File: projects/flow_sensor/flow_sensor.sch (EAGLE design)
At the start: 81 parts, among them IC1 TPS61201, IC5 REG1118

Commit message: Resubmitting work for 1/24/18
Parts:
- added U$5: LM321, my_library:LM321
- U$8: value AD8295 -> INA826; device my_library:AD8295 -> my_library:INA826
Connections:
- removed net N$35: C41.1, R8.2, R9.1
- removed net N$48: C41.2, U$8.+IN, U$8.A2-IN, U$8.A2OUT
- new net N$31: C41.1, U$5.IN-, U$5.VOUT, U$8.IN+
- new net N$36: C41.2, R8.2, R9.1
- net 3.3V: now also U$5.VCC-, U$8.IN-, U$8.REF, U$8.VS-; no longer U$8.-IN
- net N$19: now also U$5.IN+; no longer U$8.A2+IN
- net SENSOR_OUT: now also U$8.VOUT; no longer U$8.OUT
- net VCC: now also U$5.VCC+, U$8.VS+
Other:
- moved on the sheet: C41, R36
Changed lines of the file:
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@@
 <part name="U$7" library="my_library" deviceset="MAX4634" device=""/>
 <part name="GND35" library="SparkFun-PowerSymbols" deviceset="GND2" device=""/>
-<part name="U$8" library="my_library" deviceset="AD8295" device=""/>
 <part name="C41" library="SparkFun-Capacitors" deviceset="4.7UF" device="0603" value="3uF"/>
 <part name="GND36" library="SparkFun-PowerSymbols" deviceset="GND2" device=""/>
 <part name="R36" library="SparkFun-Resistors" deviceset="787OHM" device="-0603-1/10W-1%" value="600"/>
+<part name="U$5" library="my_library" deviceset="LM321" device=""/>
+<part name="GND22" library="SparkFun-PowerSymbols" deviceset="GND2" device=""/>
+<part name="U$8" library="my_library" deviceset="INA826" device=""/>
+<part name="GND28" library="SparkFun-PowerSymbols" deviceset="GND2" device=""/>
 </parts>
 <sheets>
@@
 <instance part="U$7" gate="G$1" x="254" y="5.08"/>
 <instance part="GND35" gate="G$1" x="256.54" y="27.94" rot="R180"/>
-<instance part="U$8" gate="G$1" x="337.82" y="-5.08" rot="R90"/>
-<instance part="C41" gate="G$1" x="302.26" y="15.24" rot="R90"/>
-<instance part="GND36" gate="G$1" x="322.58" y="-27.94" rot="R270"/>
-<instance part="R36" gate="G$1" x="330.2" y="-35.56"/>
+<instance part="C41" gate="G$1" x="302.26" y="-7.62" rot="R270"/>
+<instance part="GND36" gate="G$1" x="398.78" y="0" rot="R90"/>
+<instance part="R36" gate="G$1" x="383.54" y="-10.16"/>
+<instance part="U$5" gate="G$1" x="335.28" y="-2.54"/>
+<instance part="GND22" gate="G$1" x="340.36" y="-20.32"/>
+<instance part="U$8" gate="G$1" x="383.54" y="12.7" rot="R90"/>
+<instance part="GND28" gate="G$1" x="403.86" y="15.24" rot="R90"/>
 </instances>
 <busses>
@@
 <label x="251.46" y="25.4" size="1.778" layer="95" rot="R90"/>
 </segment>
+<segment>
+<wire x1="340.36" y1="7.62" x2="340.36" y2="15.24" width="0.1524" layer="91"/>
+<pinref part="U$5" gate="G$1" pin="VCC+"/>
+<label x="340.36" y="15.24" size="1.778" layer="95" rot="R90"/>
+</segment>
+<segment>
+<wire x1="375.92" y1="17.78" x2="365.76" y2="17.78" width="0.1524" layer="91"/>
+<pinref part="U$8" gate="G$1" pin="VS+"/>
+<label x="365.76" y="17.78" size="1.778" layer="95" rot="R180"/>
+</segment>
 </net>
 <net name="N$3" class="0">
@@
 </segment>
 </net>
-<net name="N$35" class="0">
-<segment>
-<pinref part="R9" gate="G$1" pin="1"/>
-<pinref part="R8" gate="G$1" pin="2"/>
-<junction x="287.02" y="0"/>
-<pinref part="C41" gate="G$1" pin="1"/>
-<wire x1="297.18" y1="15.24" x2="287.02" y2="15.24" width="0.1524" layer="91"/>
-<wire x1="287.02" y1="15.24" x2="287.02" y2="0" width="0.1524" layer="91"/>
-</segment>
-</net>
 <net name="N$19" class="0">
 <segment>
@@
 <pinref part="C28" gate="G$1" pin="1"/>
 <wire x1="297.18" y1="5.08" x2="297.18" y2="0" width="0.1524" layer="91"/>
-<wire x1="297.18" y1="0" x2="317.5" y2="0" width="0.1524" layer="91"/>
+<wire x1="297.18" y1="0" x2="322.58" y2="0" width="0.1524" layer="91"/>
 <junction x="297.18" y="0"/>
-<pinref part="U$8" gate="G$1" pin="A2+IN"/>
+<pinref part="U$5" gate="G$1" pin="IN+"/>
 </segment>
 </net>
@@
 </segment>
 <segment>
-<pinref part="U$8" gate="G$1" pin="-IN"/>
-<wire x1="325.12" y1="-22.86" x2="325.12" y2="-27.94" width="0.1524" layer="91"/>
+<pinref part="U$5" gate="G$1" pin="VCC-"/>
+<pinref part="GND22" gate="G$1" pin="3.3V"/>
+<wire x1="340.36" y1="-17.78" x2="340.36" y2="-12.7" width="0.1524" layer="91"/>
+</segment>
+<segment>
+<pinref part="U$8" gate="G$1" pin="IN-"/>
 <pinref part="GND36" gate="G$1" pin="3.3V"/>
+<wire x1="396.24" y1="0" x2="388.62" y2="0" width="0.1524" layer="91"/>
+<wire x1="388.62" y1="0" x2="388.62" y2="2.54" width="0.1524" layer="91"/>
+</segment>
+<segment>
+<pinref part="U$8" gate="G$1" pin="VS-"/>
+<pinref part="GND28" gate="G$1" pin="3.3V"/>
+<wire x1="401.32" y1="15.24" x2="401.32" y2="17.78" width="0.1524" layer="91"/>
+<wire x1="401.32" y1="17.78" x2="391.16" y2="17.78" width="0.1524" layer="91"/>
+<pinref part="U$8" gate="G$1" pin="REF"/>
+<wire x1="393.7" y1="12.7" x2="401.32" y2="12.7" width="0.1524" layer="91"/>
+<wire x1="401.32" y1="12.7" x2="401.32" y2="15.24" width="0.1524" layer="91"/>
+<junction x="401.32" y="15.24"/>
 </segment>
 </net>
@@
 </segment>
 </net>
-<net name="N$48" class="0">
-<segment>
-<pinref part="U$8" gate="G$1" pin="A2OUT"/>
-<wire x1="337.82" y1="12.7" x2="337.82" y2="15.24" width="0.1524" layer="91"/>
-<wire x1="337.82" y1="15.24" x2="317.5" y2="15.24" width="0.1524" layer="91"/>
+<net name="N$50" class="0">
+<segment>
+<pinref part="R36" gate="G$1" pin="2"/>
+<wire x1="388.62" y1="-10.16" x2="388.62" y2="-5.08" width="0.1524" layer="91"/>
+<wire x1="388.62" y1="-5.08" x2="386.08" y2="-5.08" width="0.1524" layer="91"/>
+<wire x1="386.08" y1="-5.08" x2="386.08" y2="2.54" width="0.1524" layer="91"/>
+<pinref part="U$8" gate="G$1" pin="RG'"/>
+</segment>
+</net>
+<net name="N$51" class="0">
+<segment>
+<pinref part="R36" gate="G$1" pin="1"/>
+<wire x1="378.46" y1="-10.16" x2="378.46" y2="-5.08" width="0.1524" layer="91"/>
+<wire x1="378.46" y1="-5.08" x2="381" y2="-5.08" width="0.1524" layer="91"/>
+<wire x1="381" y1="-5.08" x2="381" y2="2.54" width="0.1524" layer="91"/>
+<pinref part="U$8" gate="G$1" pin="RG"/>
+</segment>
+</net>
+<net name="SENSOR_OUT" class="0">
+<segment>
+<wire x1="383.54" y1="40.64" x2="383.54" y2="27.94" width="0.1524" layer="91"/>
+<label x="383.54" y="40.64" size="1.778" layer="95" rot="R90"/>
+<pinref part="U$8" gate="G$1" pin="VOUT"/>
+</segment>
+</net>
+<net name="N$31" class="0">
+<segment>
+<pinref part="U$5" gate="G$1" pin="VOUT"/>
+<wire x1="355.6" y1="-2.54" x2="355.6" y2="-27.94" width="0.1524" layer="91"/>
+<wire x1="355.6" y1="-27.94" x2="317.5" y2="-27.94" width="0.1524" layer="91"/>
+<pinref part="C41" gate="G$1" pin="1"/>
+<pinref part="U$5" gate="G$1" pin="IN-"/>
+<wire x1="307.34" y1="-7.62" x2="317.5" y2="-7.62" width="0.1524" layer="91"/>
+<wire x1="317.5" y1="-7.62" x2="322.58" y2="-7.62" width="0.1524" layer="91"/>
+<wire x1="317.5" y1="-27.94" x2="317.5" y2="-7.62" width="0.1524" layer="91"/>
+<junction x="317.5" y="-7.62"/>
+<wire x1="355.6" y1="-2.54" x2="378.46" y2="-2.54" width="0.1524" layer="91"/>
+<junction x="355.6" y="-2.54"/>
+<pinref part="U$8" gate="G$1" pin="IN+"/>
+<wire x1="378.46" y1="-2.54" x2="378.46" y2="2.54" width="0.1524" layer="91"/>
+</segment>
+</net>
+<net name="N$36" class="0">
+<segment>
+<pinref part="R9" gate="G$1" pin="1"/>
+<pinref part="R8" gate="G$1" pin="2"/>
+<junction x="287.02" y="0"/>
+<wire x1="287.02" y1="-7.62" x2="287.02" y2="0" width="0.1524" layer="91"/>
 <pinref part="C41" gate="G$1" pin="2"/>
-<wire x1="317.5" y1="15.24" x2="304.8" y2="15.24" width="0.1524" layer="91"/>
-<wire x1="337.82" y1="15.24" x2="360.68" y2="15.24" width="0.1524" layer="91"/>
-<wire x1="360.68" y1="15.24" x2="360.68" y2="-27.94" width="0.1524" layer="91"/>
-<junction x="337.82" y="15.24"/>
-<wire x1="360.68" y1="-27.94" x2="335.28" y2="-27.94" width="0.1524" layer="91"/>
-<pinref part="U$8" gate="G$1" pin="+IN"/>
-<wire x1="335.28" y1="-27.94" x2="335.28" y2="-22.86" width="0.1524" layer="91"/>
-<pinref part="U$8" gate="G$1" pin="A2-IN"/>
-<wire x1="317.5" y1="5.08" x2="317.5" y2="15.24" width="0.1524" layer="91"/>
-<junction x="317.5" y="15.24"/>
-</segment>
-</net>
-<net name="N$50" class="0">
-<segment>
-<pinref part="R36" gate="G$1" pin="2"/>
-<wire x1="335.28" y1="-35.56" x2="335.28" y2="-30.48" width="0.1524" layer="91"/>
-<wire x1="335.28" y1="-30.48" x2="332.74" y2="-30.48" width="0.1524" layer="91"/>
-<pinref part="U$8" gate="G$1" pin="RG'"/>
-<wire x1="332.74" y1="-30.48" x2="332.74" y2="-22.86" width="0.1524" layer="91"/>
-</segment>
-</net>
-<net name="N$51" class="0">
-<segment>
-<pinref part="R36" gate="G$1" pin="1"/>
-<wire x1="325.12" y1="-35.56" x2="325.12" y2="-30.48" width="0.1524" layer="91"/>
-<wire x1="325.12" y1="-30.48" x2="327.66" y2="-30.48" width="0.1524" layer="91"/>
-<pinref part="U$8" gate="G$1" pin="RG"/>
-<wire x1="327.66" y1="-30.48" x2="327.66" y2="-22.86" width="0.1524" layer="91"/>
-</segment>
-</net>
-<net name="SENSOR_OUT" class="0">
-<segment>
-<pinref part="U$8" gate="G$1" pin="OUT"/>
-<wire x1="317.5" y1="-5.08" x2="302.26" y2="-5.08" width="0.1524" layer="91"/>
-<wire x1="302.26" y1="-5.08" x2="302.26" y2="-15.24" width="0.1524" layer="91"/>
-<label x="302.26" y="-15.24" size="1.778" layer="95" rot="R270"/>
-</segment>
-</net>
+<wire x1="287.02" y1="-7.62" x2="299.72" y2="-7.62" width="0.1524" layer="91"/>
+</segment>
+</net>

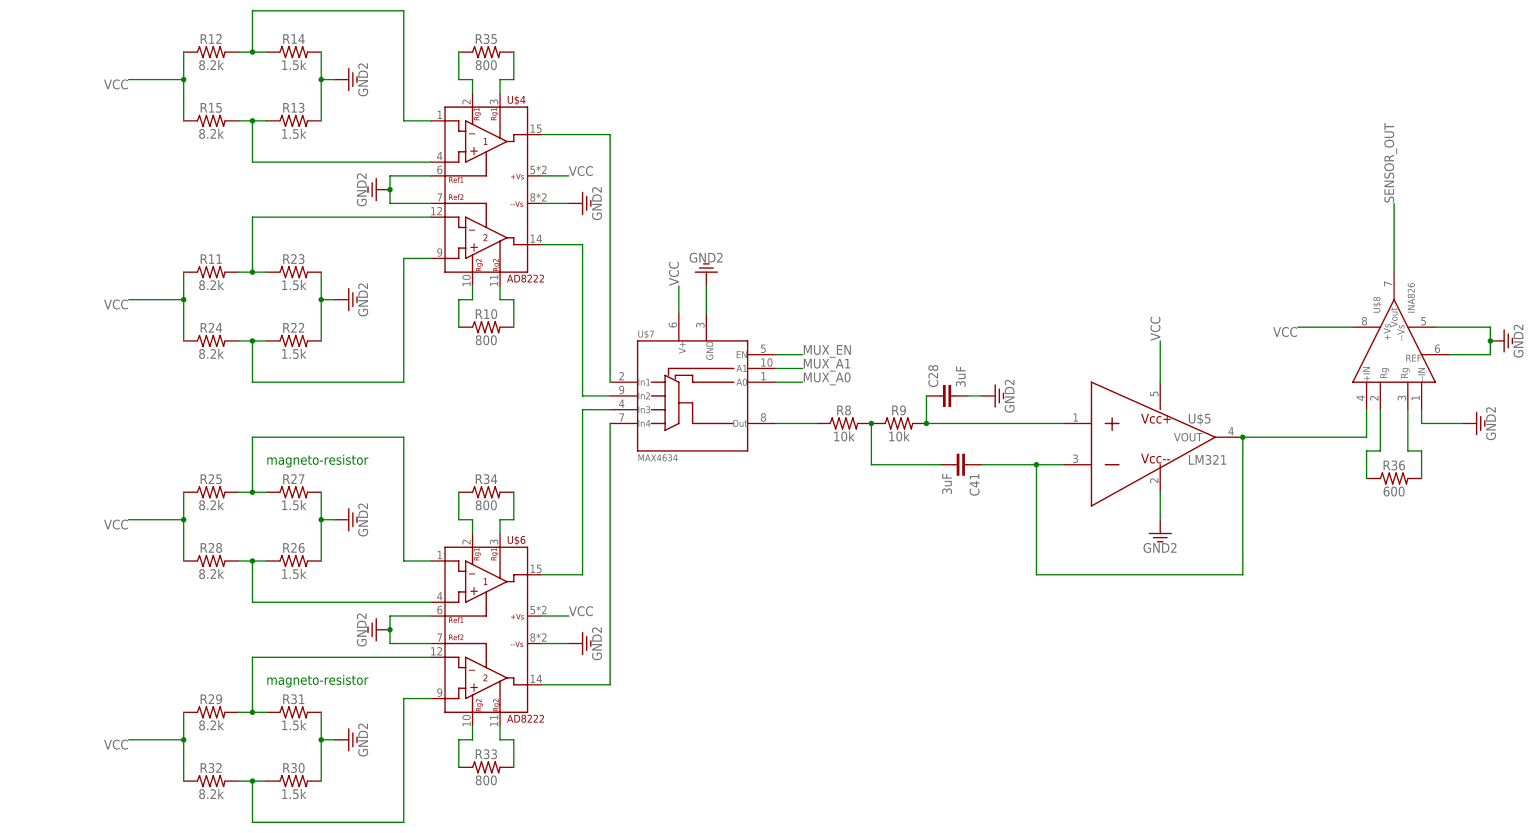
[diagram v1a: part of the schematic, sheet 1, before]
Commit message: Changed sensor schematic to have 1 wheatstone bridge with 4 sensors
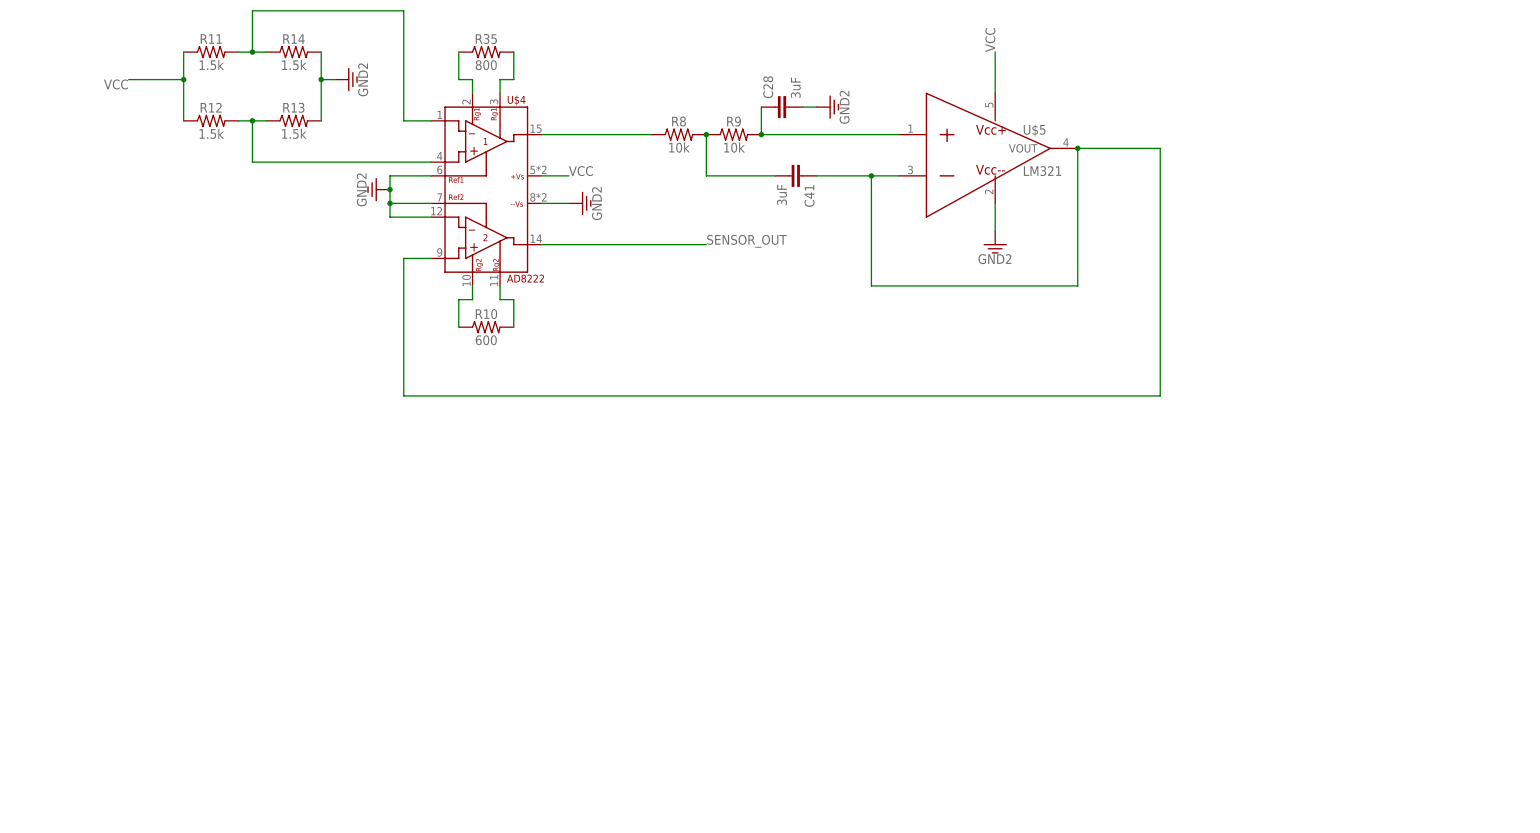
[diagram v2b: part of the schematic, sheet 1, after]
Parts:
- removed R15, R24, R28, R32: 8.2k, SparkFun-Resistors:1.5KOHM-0603-1/10W-1%
- removed R22, R26, R30: 1.5k, SparkFun-Resistors:8.2KOHM-0603-1/10W-5%
- removed R23, R27, R31: 1.5k, SparkFun-Resistors:1.5KOHM-0603-1/10W-1%
- removed R25, R29: 8.2k, SparkFun-Resistors:8.2KOHM-0603-1/10W-5%
- removed R33, R34: 800, SparkFun-Resistors:787OHM-0603-1/10W-1%
- removed R36: 600, SparkFun-Resistors:787OHM-0603-1/10W-1%
- removed U$6: AD8222, my_library:AD8222
- removed U$7: MAX4634, my_library:MAX4634
- removed U$8: INA826, my_library:INA826
- R10: value 800 -> 600
- R11: value 8.2k -> 1.5k; device SparkFun-Resistors:8.2KOHM-0603-1/10W-5% -> SparkFun-Resistors:1.5KOHM-0603-1/10W-1%
- R12: value 8.2k -> 1.5k
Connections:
- removed net MUX_A0: U$7.A0
- removed net MUX_A1: U$7.A1
- removed net MUX_EN: U$7.EN
- removed net N$1: R11.2, R23.1, U$4.-IN2
- removed net N$18: R8.1, U$7.COM
- removed net N$22: R25.2, R27.1, U$6.-IN1
- removed net N$25: R26.1, R28.2, U$6.+IN1
- removed net N$26: R29.2, R31.1, U$6.-IN2
- removed net N$27: R30.1, R32.2, U$6.+IN2
- removed net N$30: R33.1, U$6.RG2
- removed net N$31: C41.1, U$5.IN-, U$5.VOUT, U$8.IN+
- removed net N$32: R33.2, U$6.RG2'
- removed net N$33: R34.1, U$6.RG1
- removed net N$34: R34.2, U$6.RG1'
- removed net N$44: U$4.OUT2, U$7.NO2
- removed net N$45: U$6.OUT1, U$7.NO3
- removed net N$46: U$6.OUT2, U$7.NO4
- removed net N$50: R36.2, U$8.RG'
- removed net N$51: R36.1, U$8.RG
- net 3.3V: no longer U$7.GND, U$8.IN-, U$8.REF, U$8.VS-
- net GND: now also U$4.-IN2; no longer R22.2, R23.2, R26.2, R27.2, R30.2, R31.2, U$6.-VS, U$6.REF1, U$6.REF2
- net N$21: now also C41.1, U$5.IN-, U$5.VOUT; no longer R22.1, R24.2
- net N$28: now also R11.2; no longer R12.2
- net N$29: now also R12.2; no longer R15.2
- net N$37: now also U$4.RG1
- net N$40: now also U$4.RG1'
- net N$43: now also R8.1; no longer U$7.NO1
- net SENSOR_OUT: now also U$4.OUT2; no longer U$8.VOUT
- net VCC: no longer R15.1, R24.1, R25.1, R28.1, R29.1, R32.1, U$6.+VS, U$7.V+, U$8.VS+
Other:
- note removed: "magneto-resistor"
- moved on the sheet: C28, C41, R11, R12, R8, R9, U$5
